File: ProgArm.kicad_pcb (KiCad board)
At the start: 2 copper layers, 40 x 50 mm, 130 parts, among them M1 MOTOR, P1 I²C_Port, P10 TXD, P11 RING_VCC, P12 RING_GND, P13 RING_GPIOA_3_Port, P14 RING_GPIOA_4_Port, P15 RXD, P16 RING_BUTTONS_Port, P17 MicroUSB, P2 SPI_Port, P3 UART_Port, P4 SWD_Port, P5 GPIOA_1_2_Port, P6 TIM1_Port, P7 T_SENS, P8 RING_IR_OUT, P9 RING_LEDS_Port, Q1 MOS_P, Q2 MOS_P, Q3 MOS_P, Q4 MOS_P, Q5 MOS_P, Q6 MOS_P, Q7 MOS_P, Q8 MOS_P, SW1 FW/RST, SW2 ON/OFF, U1 TPS78330, U2 BQ24297, U3 LM3668, U4 STM32F103R, U5 MPU9250, U6 BQ27410, U7 SI1143, U8 LPS25H, U9 NRF8001, X1 32.768kHz, X2 8MHz, X3 16MHz

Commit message: Arranged blocks
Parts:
- moved R36 70.5 mm to (145.0, 62.4)
- moved R37 70.5 mm to (145.0, 63.5)
- moved R35 70.5 mm to (145.0, 64.6)
- moved R9 70.5 mm to (145.0, 60.4), turned to 180 degrees
- moved R33 70.4 mm to (138.8, 53.6)
- moved R34 70.3 mm to (137.7, 53.6)
- moved U4 70.2 mm to (136.7, 62.3)
- moved C4 70.1 mm to (128.5, 64.0), turned to 180 degrees
- moved C12 70.1 mm to (135.0, 75.2), turned to 0 degrees
- moved X2 69.0 mm to (137.7, 73.6), turned to 90 degrees
- moved C6 69.0 mm to (133.3, 76.3), turned to 0 degrees
- moved X1 69.0 mm to (134.1, 72.7), turned to 270 degrees
- moved U1 68.3 mm to (128.4, 71.7), turned to 0 degrees
- moved C9 66.7 mm to (129.0, 69.2), turned to 180 degrees
- moved C16 65.2 mm to (36.8, 58.5), turned to 90 degrees
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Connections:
- X3 pad 0: (no net) -> GND
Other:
- net class Default: clearance 0.2 -> 0.199999
- rule trace_clearance: 0.2 -> 0.199999

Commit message: Routed! 105 vias, 2,501,678
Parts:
- moved R9 82.0 mm to (64.8, 77.3), turned to 0 degrees
- moved R36 81.3 mm to (64.8, 75.3), turned to 180 degrees
- moved R37 81.0 mm to (64.8, 74.2), turned to 180 degrees
- moved R35 80.7 mm to (64.8, 73.2), turned to 180 degrees
- moved R33 74.4 mm to (71.0, 84.2), turned to 270 degrees
- moved R34 72.4 mm to (72.0, 84.2), turned to 270 degrees
- moved X2 66.3 mm to (72.0, 64.2), turned to 270 degrees
- moved U4 65.0 mm to (73.0, 75.5), turned to 180 degrees
- moved C11 62.1 mm to (74.8, 61.5), turned to 180 degrees
- moved C12 61.6 mm to (74.8, 62.5), turned to 180 degrees
- moved X1 58.9 mm to (75.7, 65.0), turned to 90 degrees
- moved C6 58.8 mm to (76.5, 61.5), turned to 180 degrees
- moved C10 58.2 mm to (76.5, 62.5), turned to 180 degrees
- moved C19 51.5 mm to (59.2, 61.0), turned to 0 degrees
- moved C5 49.3 mm to (80.8, 63.5), turned to 0 degrees
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
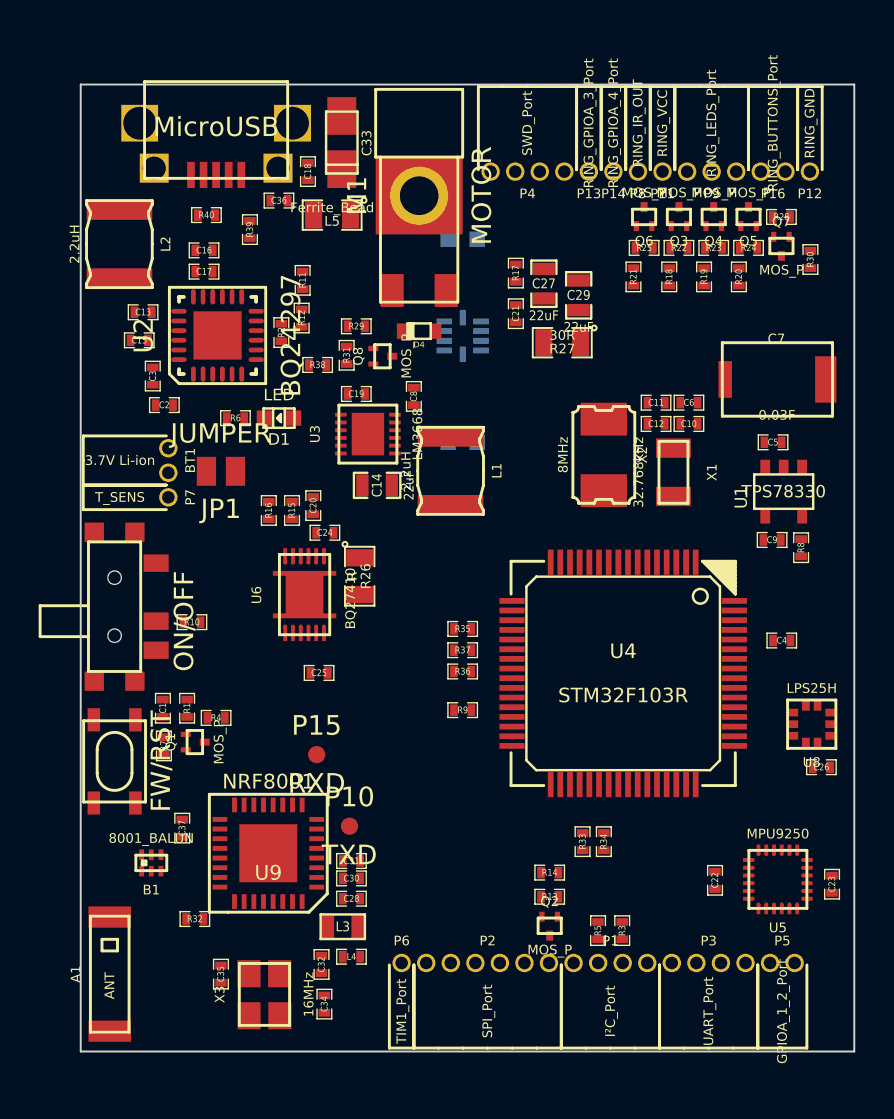
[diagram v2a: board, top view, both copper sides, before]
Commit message: Small fixed, tracks imported
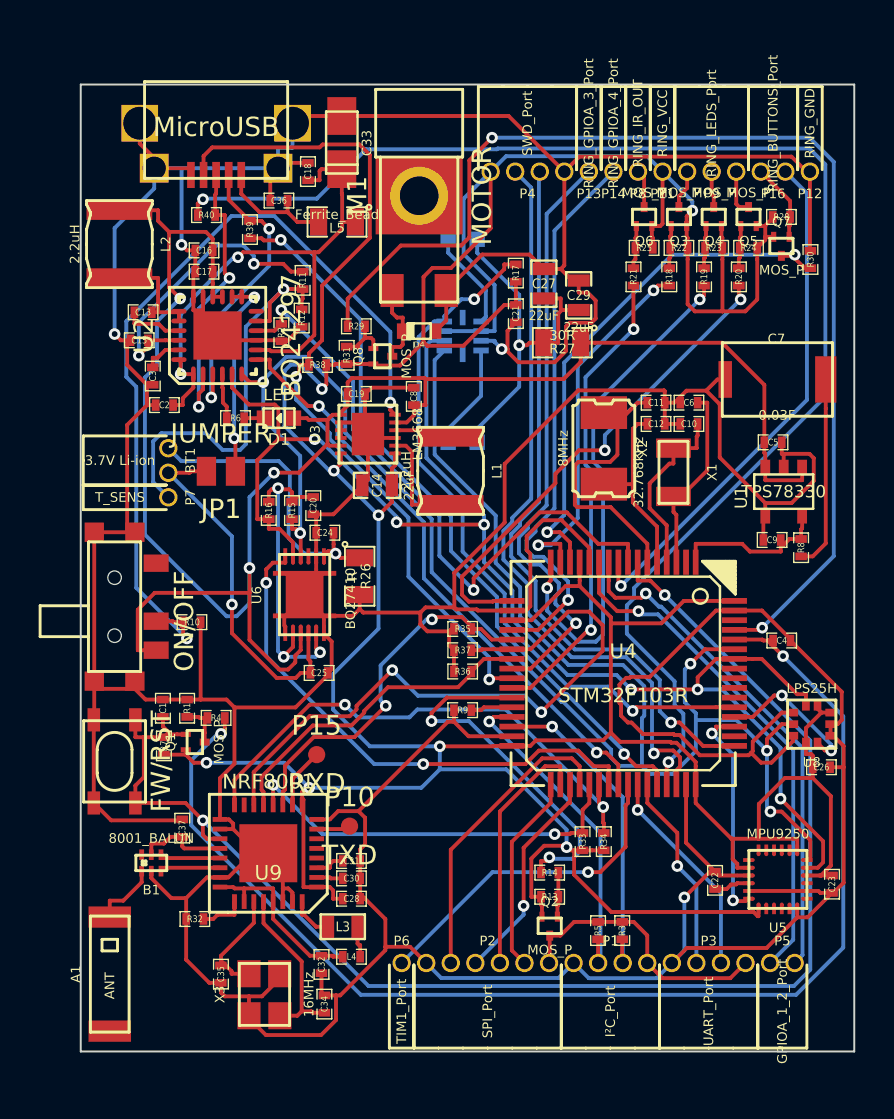
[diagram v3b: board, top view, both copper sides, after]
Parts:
- moved L5 0.44 mm to (58.3, 52.1)
- moved X2 0.34 mm to (72.0, 63.8)
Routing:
- net GND: track 0.00 -> 402.1 mm, vias 0 -> 4
- net +3.3V: track 0.00 -> 223.6 mm, vias 0 -> 8
- net VCC: track 0.00 -> 103.5 mm, vias 0 -> 3
- net SDA: track 0.00 -> 97.0 mm, vias 0 -> 5
- net SCL: track 0.00 -> 75.7 mm, vias 0 -> 6
- net ~RESET: track 0.00 -> 74.7 mm, vias 0 -> 2
- net D+: track 0.00 -> 72.5 mm, vias 0 -> 2
- net N-0000085: track 0.00 -> 64.2 mm, vias 0 -> 2
- net ~VIBRATION: track 0.00 -> 60.0 mm, vias 0 -> 2
- net ~OTG_cable: track 0.00 -> 44.4 mm, vias 0 -> 2
- net N-0000033: track 0.00 -> 42.8 mm, vias 0 -> 2
- net SWDIO: track 0.00 -> 38.9 mm, vias 0 -> 1
- net D-: track 0.00 -> 38.4 mm, vias 0 -> 2
- net SWCLK: track 0.00 -> 37.9 mm, vias 0 -> 1
- net ~SI_INT: track 0.00 -> 37.4 mm, vias 0 -> 2
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
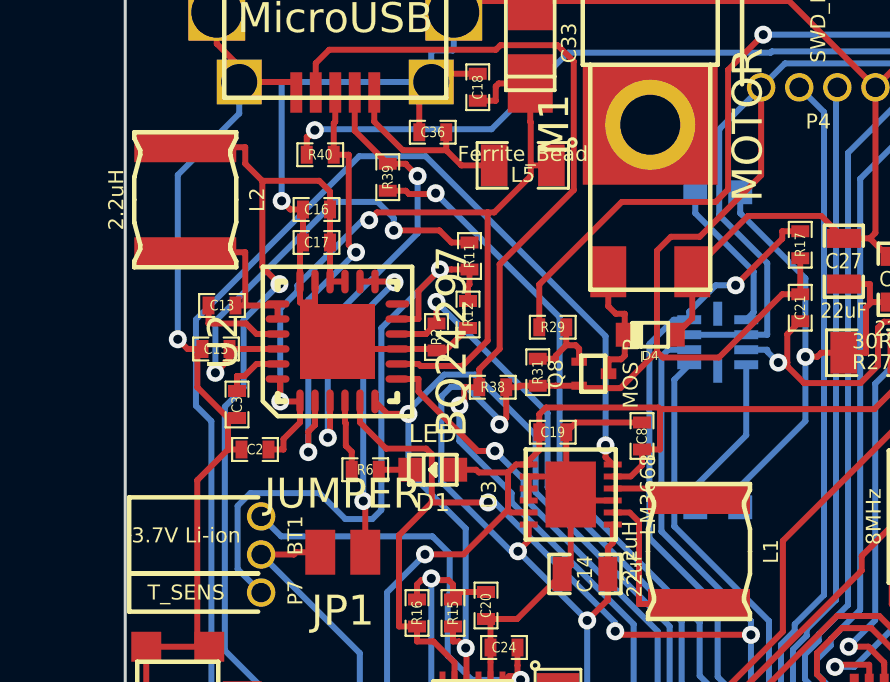
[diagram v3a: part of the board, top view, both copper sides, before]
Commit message: Footprints changed according to 8f30ef2
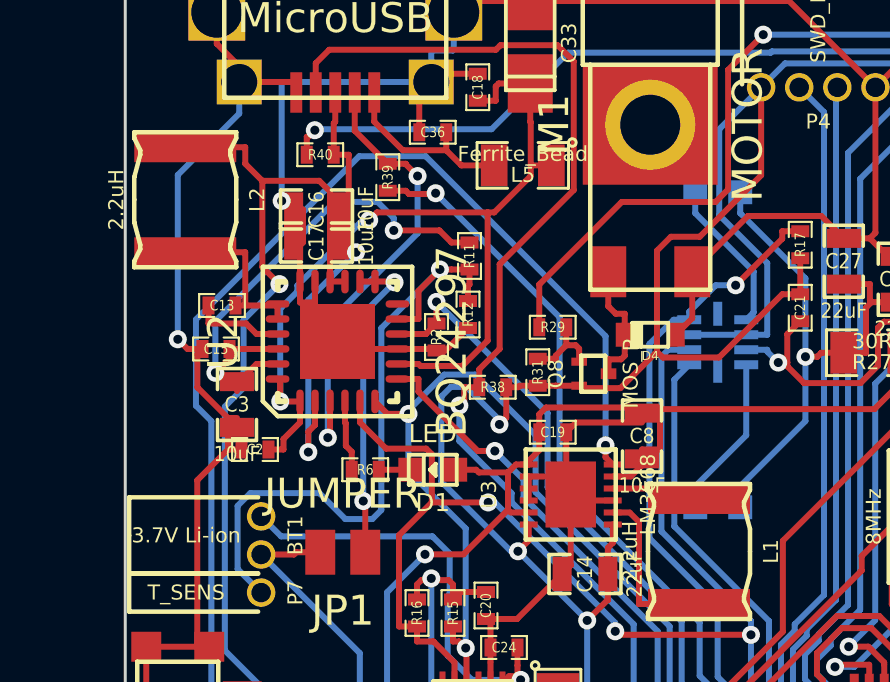
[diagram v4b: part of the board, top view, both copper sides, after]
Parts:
- C16, C17, C3, C8: footprint SM0402_c -> SM0603_Capa

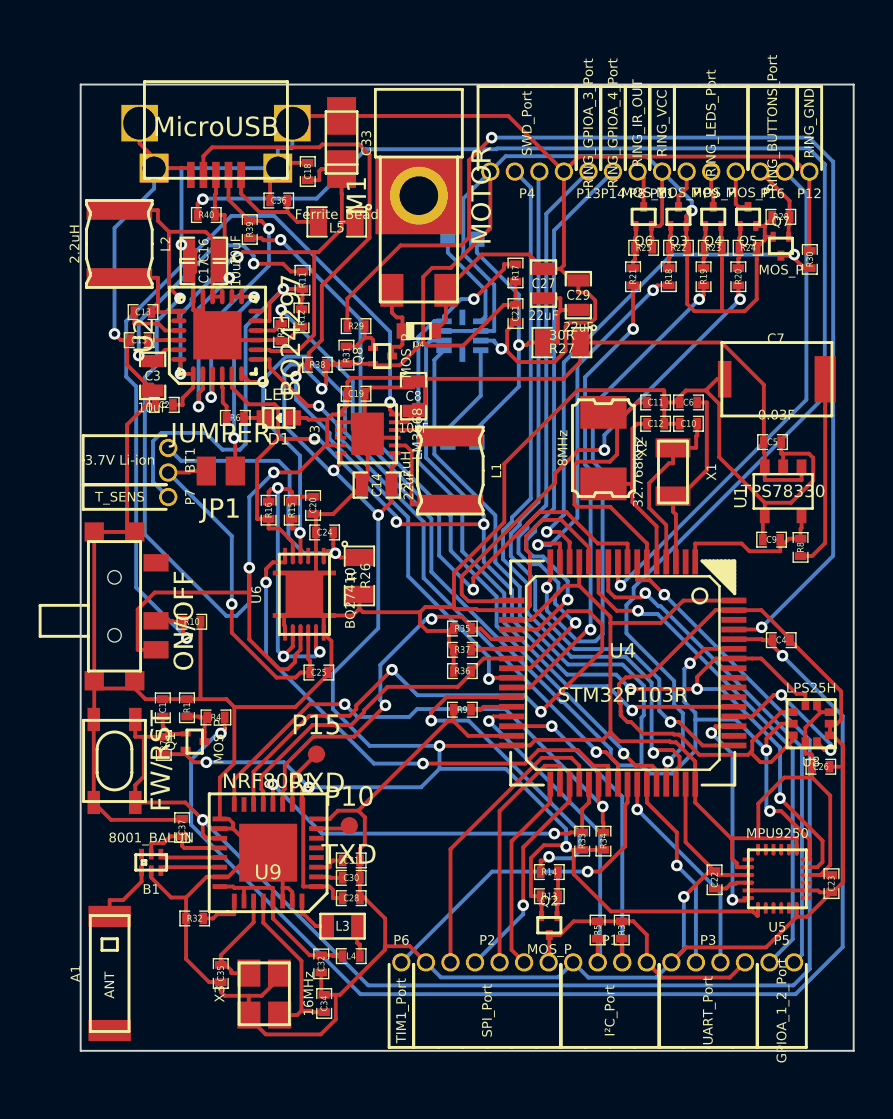
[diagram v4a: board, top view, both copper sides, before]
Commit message: Small fixes, thick power traces
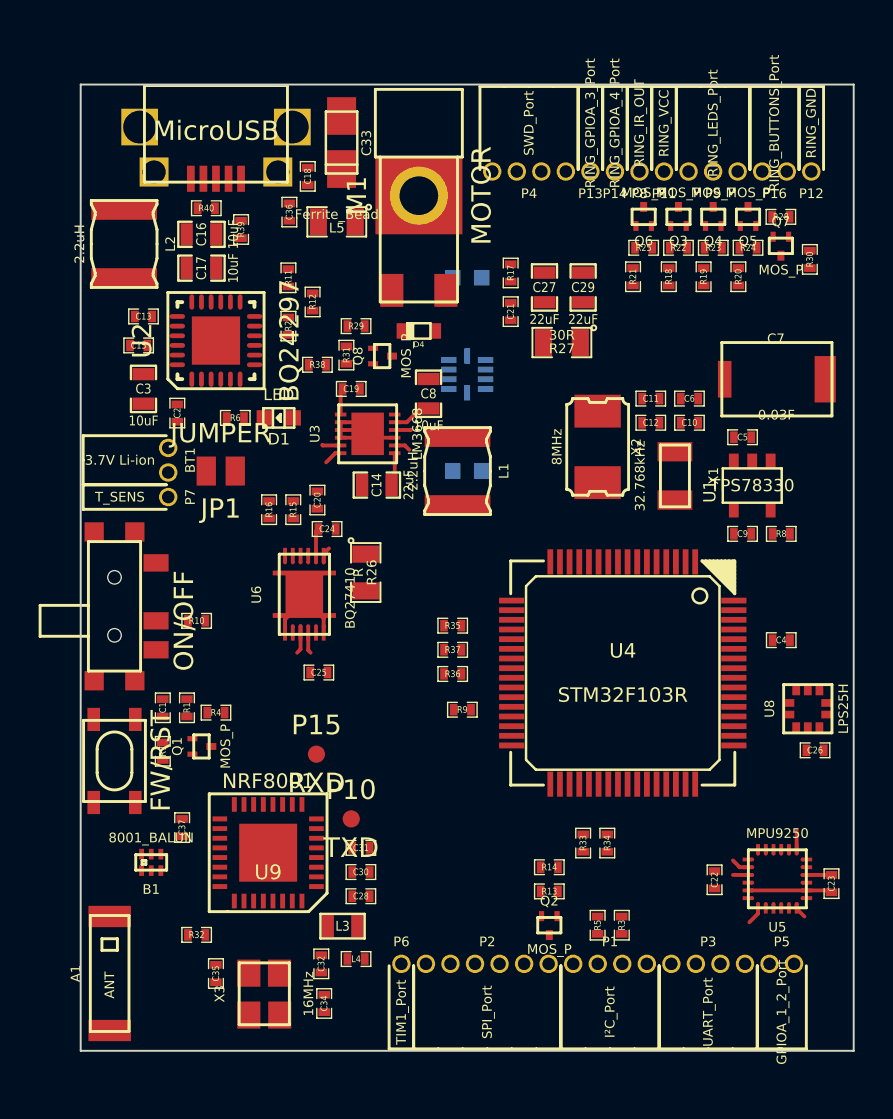
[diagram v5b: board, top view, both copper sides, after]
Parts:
- moved D3 2.02 mm to (65.0, 55.0)
- moved U7 2.02 mm to (65.0, 60.0)
- moved U1 1.63 mm to (79.8, 65.8)
- moved C5 1.57 mm to (79.2, 63.2)
- moved C9 1.53 mm to (79.2, 68.2)
- moved D2 1.52 mm to (65.0, 65.0)
- moved R8 1.22 mm to (81.2, 68.2), turned to 180 degrees
- moved R12 1.01 mm to (57.0, 56.2)
- moved C26 0.90 mm to (83.0, 79.5), turned to 180 degrees
- moved R32 0.86 mm to (51.0, 89.0)
- moved C16 0.83 mm to (51.2, 52.8)
- moved C3 0.83 mm to (48.2, 60.8)
- moved C31 0.82 mm to (59.5, 84.5)
- moved C36 0.81 mm to (55.8, 51.6), turned to 90 degrees
- moved C2 0.80 mm to (50.0, 62.0), turned to 270 degrees
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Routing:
- net GND: track 402.1 -> 19.5 mm, vias 4 -> 0
- net +3.3V: track 223.6 -> 7.15 mm, vias 8 -> 0
- net VCC: track 103.5 -> 5.82 mm, vias 3 -> 0
- net SDA: track 97.0 -> 0.00 mm, vias 5 -> 0
- net SCL: track 75.7 -> 0.00 mm, vias 6 -> 0
- net ~RESET: track 74.7 -> 0.00 mm, vias 2 -> 0
- net D+: track 72.5 -> 0.00 mm, vias 2 -> 0
- net N-0000085: track 64.2 -> 0.00 mm, vias 2 -> 0
- net ~VIBRATION: track 60.0 -> 0.00 mm, vias 2 -> 0
- net ~OTG_cable: track 44.4 -> 0.00 mm, vias 2 -> 0
- net N-0000033: track 42.8 -> 0.00 mm, vias 2 -> 0
- net SWDIO: track 38.9 -> 0.00 mm, vias 1 -> 0
- net D-: track 38.4 -> 0.00 mm, vias 2 -> 0
- net SWCLK: track 37.9 -> 0.00 mm, vias 1 -> 0
- net ~SI_INT: track 37.4 -> 0.00 mm, vias 2 -> 0
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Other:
- net class Power: clearance 0.2 -> 0.199999; trace_width 0.3 -> 0.295

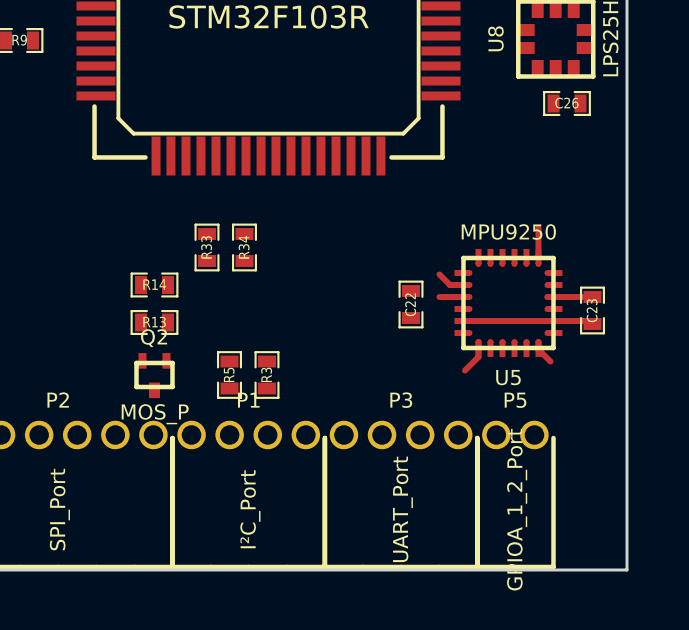
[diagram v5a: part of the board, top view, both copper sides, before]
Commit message: Board Optimized: Via count: 100  Trace Lenght: 2,515,295,8805
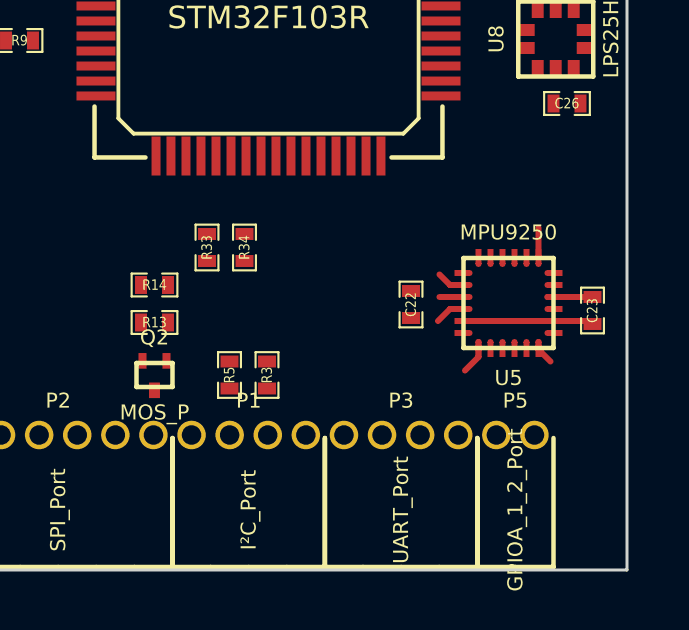
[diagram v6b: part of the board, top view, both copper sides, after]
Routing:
- net N-000006: track 0.00 -> 0.97 mm
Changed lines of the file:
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@@
-(kicad_pcb (version 3) (host pcbnew "(25-Oct-2014 BZR 4029)-stable")
+(kicad_pcb (version 3) (host pcbnew "(2013-07-07 BZR 4022)-stable")
   (general
     (links 365)
     (no_connects 329)
-    (area 42.624999 42.018278 85.050001 97.075388)
+    (area 42.625 42.015279 85.050001 97.151387)
     (thickness 1.6)
     (drawings 4)
-    (tracks 61)
+    (tracks 63)
     (zones 0)
     (modules 130)
@@
   (segment (start 61.25 62.875) (end 62.075 62.875) (width 0.2) (layer F.Cu) (net 52))
   (segment (start 62.075 62.875) (end 62.1 62.85) (width 0.2) (layer F.Cu) (net 52))
+  (segment (start 79.5 86.3) (end 79.1 86.3) (width 0.2) (layer F.Cu) (net 59) (status 400000))
+  (segment (start 79.1 86.3) (end 78.7 86.7) (width 0.2) (layer F.Cu) (net 59))
   (segment (start 61.25 62.475) (end 61.875 62.475) (width 0.2) (layer F.Cu) (net 88))
   (segment (start 62.588 61.762) (end 63 61.762) (width 0.2) (layer F.Cu) (net 88))
